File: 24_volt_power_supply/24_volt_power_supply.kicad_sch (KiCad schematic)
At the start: 12 parts, among them J1 Conn_01x02_Pin, J2 Screw_Terminal_01x02, J3 Conn_01x02_Pin, J4 Conn_01x03_Pin, K1 Relay_SPDT

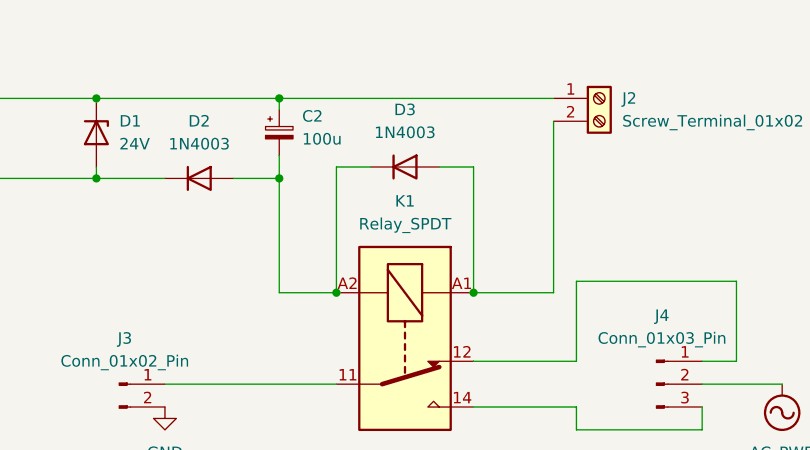
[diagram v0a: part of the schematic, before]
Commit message: fixed freewheeling diode direction
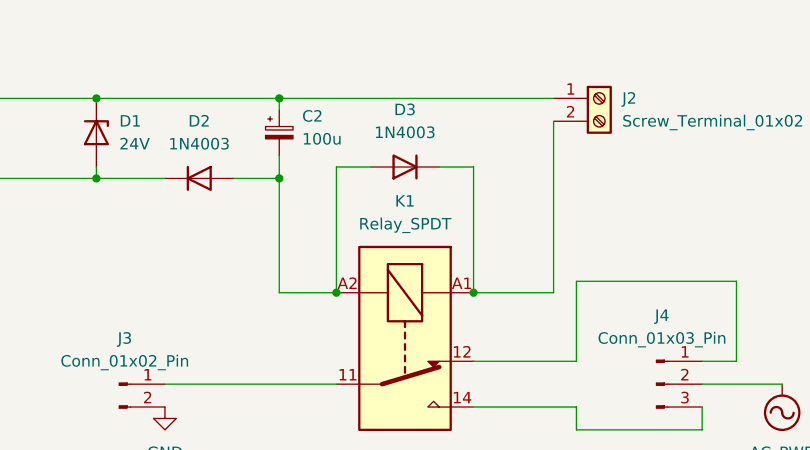
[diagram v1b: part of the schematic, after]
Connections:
- net at J2.2 (Pin_2), K1.A1: now also D3.1 (K); no longer D3.2 (A)
- net at C2.2, D2.2 (A), K1.A2: now also D3.2 (A); no longer D3.1 (K)
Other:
- moved on the sheet: D3
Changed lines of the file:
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@@
 	(symbol
 		(lib_id "Diode:1N4003")
-		(at 166.37 62.23 0)
+		(at 166.37 62.23 180)
 		(unit 1)
 		(exclude_from_sim no)
@@
 		)
 		(property "Footprint" "Diode_THT:D_DO-41_SOD81_P10.16mm_Horizontal"
-			(at 166.37 66.675 0)
+			(at 166.37 57.785 0)
 			(effects
 				(font

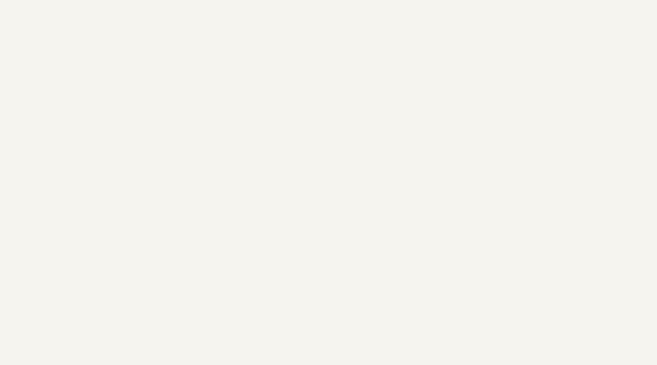
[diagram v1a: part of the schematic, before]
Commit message: started mounting holes for pcb
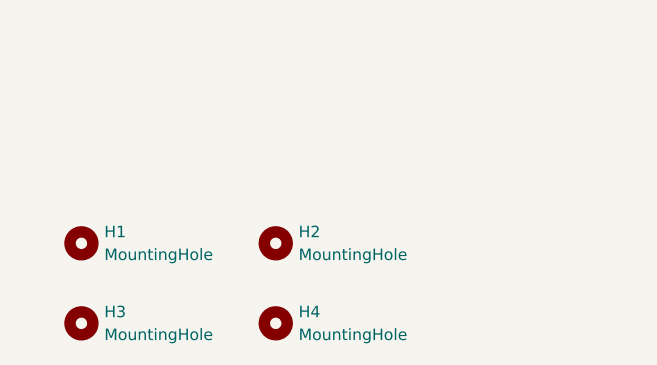
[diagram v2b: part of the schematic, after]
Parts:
- added H1, H2, H3, H4: MountingHole, MountingHole:MountingHole_3.2mm_M3_ISO14580_Pad_TopOnly, symbol Mechanical:MountingHole
